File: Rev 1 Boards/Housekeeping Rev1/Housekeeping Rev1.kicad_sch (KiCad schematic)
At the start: 0 parts

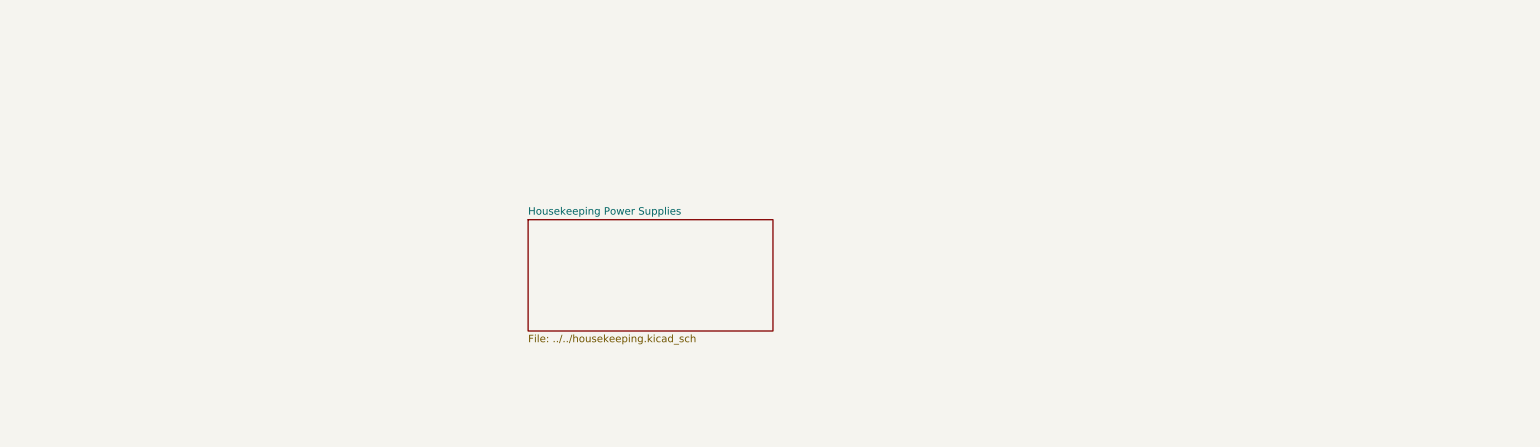
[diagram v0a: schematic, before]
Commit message: added footprints to prepare for pcb layout
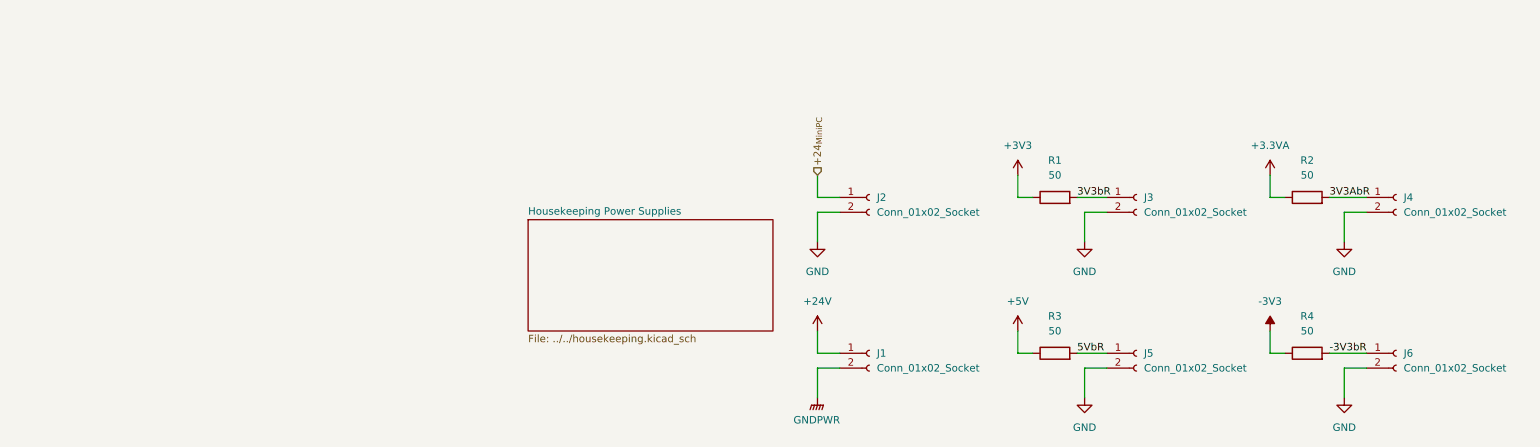
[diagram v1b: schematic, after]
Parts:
- added J1, J2: Conn_01x02_Socket, Connector:Banana_Jack_2Pin, symbol Connector:Conn_01x02_Socket
- added J3, J4, J5, J6: Conn_01x02_Socket, symbol Connector:Conn_01x02_Socket
- added R1, R2, R3, R4: 50, symbol Device:R
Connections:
- new net +24V: J1.1 (Pin_1)
- new net +24_{MiniPC}: J2.1 (Pin_1)
- new net +3.3VA: R2.1
- new net +3V3: R1.1
- new net +5V: R3.1
- new net -3V3: R4.1
- new net -3V3bR: J6.1 (Pin_1), R4.2
- new net 3V3AbR: J4.1 (Pin_1), R2.2
- new net 3V3bR: J3.1 (Pin_1), R1.2
- new net 5VbR: J5.1 (Pin_1), R3.2
- new net GND: J2.2 (Pin_2), J3.2 (Pin_2), J4.2 (Pin_2), J5.2 (Pin_2), J6.2 (Pin_2)
- new net GNDPWR: J1.2 (Pin_2)

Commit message: assigned footprints, mouser part numbers, and datasheets for passive components
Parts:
- J3, J4, J5, J6: footprint (none) -> Connector:Banana_Jack_2Pin
- R1, R2, R3, R4: footprint (none) -> Resistor_SMD:R_0201_0603Metric_Pad0.64x0.40mm_HandSolder; Mouser Part Number (none) -> 71-TNPW060350R0DEEA
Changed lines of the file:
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@@
 			)
 		)
-		(property "Footprint" ""
+		(property "Footprint" "Resistor_SMD:R_0201_0603Metric_Pad0.64x0.40mm_HandSolder"
 			(at 187.96 102.108 90)
 			(effects
@@
 			)
 		)
-		(property "Datasheet" "~"
+		(property "Datasheet" "https://www.vishay.com/docs/28758/tnpw_e3.pdf"
 			(at 187.96 100.33 0)
 			(effects
@@
 			)
 		)
+		(property "Mouser Part Number" "71-TNPW060350R0DEEA"
+			(at 187.96 100.33 0)
+			(effects
+				(font
+					(size 1.27 1.27)
+				)
+				(hide yes)
+			)
+		)
 		(pin "1"
 		)
@@
 			)
 		)
-		(property "Footprint" ""
+		(property "Footprint" "Resistor_SMD:R_0201_0603Metric_Pad0.64x0.40mm_HandSolder"
 			(at 187.96 75.438 90)
 			(effects
@@
 			)
 		)
-		(property "Datasheet" "~"
+		(property "Datasheet" "https://www.vishay.com/docs/28758/tnpw_e3.pdf"
 			(at 187.96 73.66 0)
 			(effects
@@
 			)
 		)
+		(property "Mouser Part Number" "71-TNPW060350R0DEEA"
+			(at 187.96 73.66 0)
+			(effects
+				(font
+					(size 1.27 1.27)
+				)
+				(hide yes)
+			)
+		)
 		(pin "1"
 		)
@@
 			)
 		)
-		(property "Footprint" ""
+		(property "Footprint" "Connector:Banana_Jack_2Pin"
 			(at 246.38 100.33 0)
 			(effects
@@
 			)
 		)
-		(property "Footprint" ""
+		(property "Footprint" "Resistor_SMD:R_0201_0603Metric_Pad0.64x0.40mm_HandSolder"
 			(at 231.14 102.108 90)
 			(effects
@@
 			)
 		)
-		(property "Datasheet" "~"
+		(property "Datasheet" "https://www.vishay.com/docs/28758/tnpw_e3.pdf"
 			(at 231.14 100.33 0)
 			(effects
@@
 			)
 		)
+		(property "Mouser Part Number" "71-TNPW060350R0DEEA"
+			(at 231.14 100.33 0)
+			(effects
+				(font
+					(size 1.27 1.27)
+				)
+				(hide yes)
+			)
+		)
 		(pin "1"
 		)
@@
 			)
 		)
-		(property "Footprint" ""
+		(property "Footprint" "Connector:Banana_Jack_2Pin"
 			(at 201.93 100.33 0)
 			(effects
@@
 			)
 		)
-		(property "Footprint" ""
+		(property "Footprint" "Connector:Banana_Jack_2Pin"
 			(at 246.38 73.66 0)
 			(effects
@@
 			)
 		)
-		(property "Footprint" ""
+		(property "Footprint" "Connector:Banana_Jack_2Pin"
 			(at 201.93 73.66 0)
 			(effects
@@
 			)
 		)
-		(property "Footprint" ""
+		(property "Footprint" "Resistor_SMD:R_0201_0603Metric_Pad0.64x0.40mm_HandSolder"
 			(at 231.14 75.438 90)
 			(effects
@@
 			)
 		)
-		(property "Datasheet" "~"
+		(property "Datasheet" "https://www.vishay.com/docs/28758/tnpw_e3.pdf"
 			(at 231.14 73.66 0)
 			(effects
@@
 			(at 231.14 73.66 0)
 			(effects
+				(font
+					(size 1.27 1.27)
+				)
+				(hide yes)
+			)
+		)
+		(property "Mouser Part Number" "71-TNPW060350R0DEEA"
+			(at 231.14 73.66 0)
+			(effects

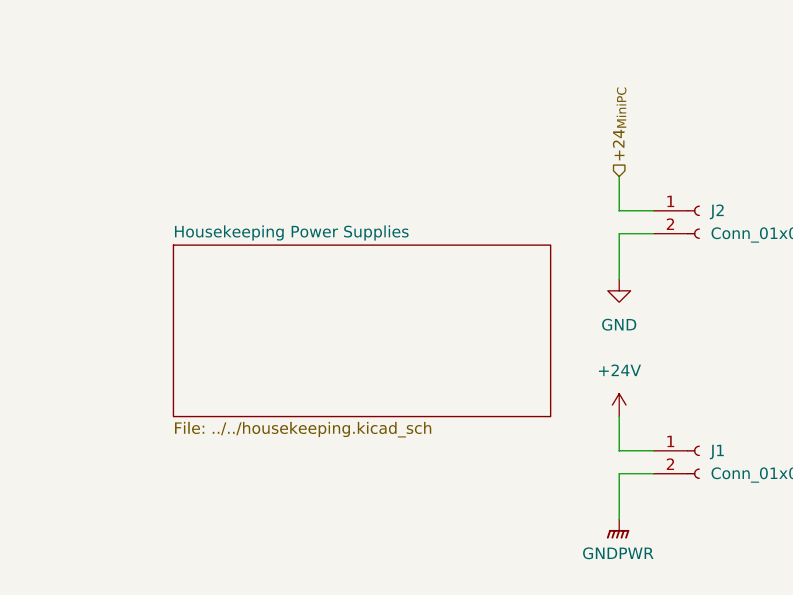
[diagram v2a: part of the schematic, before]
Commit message: beginning layout work for housekeeping pcb
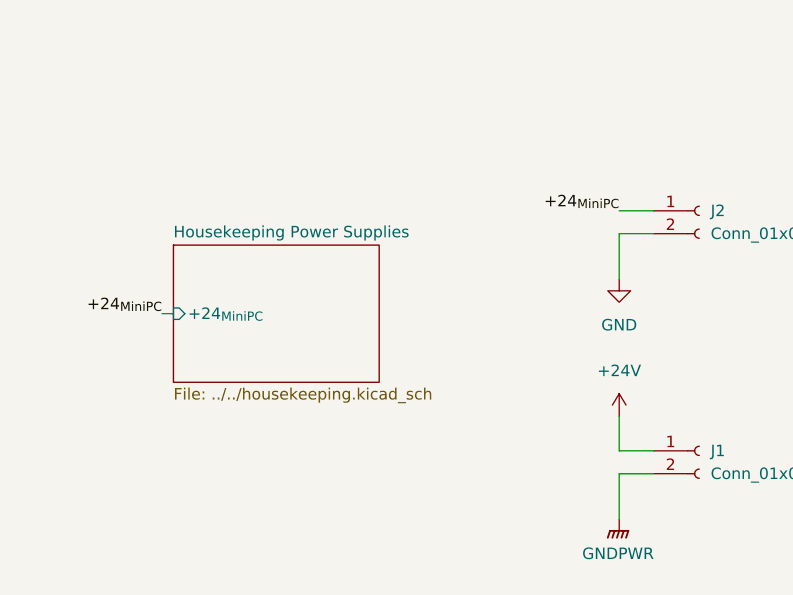
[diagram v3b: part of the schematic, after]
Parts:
- R1, R2, R3, R4: footprint Resistor_SMD:R_0201_0603Metric_Pad0.64x0.40mm_HandSolder -> Resistor_SMD:R_0603_1608Metric_Pad0.98x0.95mm_HandSolder
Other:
- sheet Housekeeping Power Supplies ports: added +24_{MiniPC}; removed none
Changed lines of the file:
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@@
-	(wire
-		(pts
-			(xy 147.32 69.85) (xy 147.32 73.66)
-		)
-		(stroke
-			(width 0)
-			(type default)
-		)
-	)
 	(wire
 		(pts
@@
 		(pts
 			(xy 237.49 102.87) (xy 237.49 107.95)
+		)
+		(stroke
+			(width 0)
+			(type default)
+		)
+	)
+	(wire
+		(pts
+			(xy 96.52 85.09) (xy 97.79 85.09)
 		)
 		(stroke
@@
 		)
 	)
+	(label "+24_{MiniPC}"
+		(at 96.52 85.09 180)
+		(effects
+			(font
+				(size 1.27 1.27)
+			)
+			(justify right bottom)
+		)
+	)
 	(label "5VbR"
 		(at 191.77 100.33 0)
@@
 		)
 	)
-	(hierarchical_label "+24_{MiniPC}"
-		(shape input)
-		(at 147.32 69.85 90)
+	(label "+24_{MiniPC}"
+		(at 147.32 73.66 180)
 		(effects
 			(font
 				(size 1.27 1.27)
 			)
-			(justify left)
+			(justify right bottom)
 		)
 	)
@@
 			)
 		)
-		(property "Footprint" "Resistor_SMD:R_0201_0603Metric_Pad0.64x0.40mm_HandSolder"
+		(property "Footprint" "Resistor_SMD:R_0603_1608Metric_Pad0.98x0.95mm_HandSolder"
 			(at 187.96 102.108 90)
 			(effects
@@
 			)
 		)
-		(property "Footprint" "Resistor_SMD:R_0201_0603Metric_Pad0.64x0.40mm_HandSolder"
+		(property "Footprint" "Resistor_SMD:R_0603_1608Metric_Pad0.98x0.95mm_HandSolder"
 			(at 187.96 75.438 90)
 			(effects
@@
 			)
 		)
-		(property "Footprint" "Resistor_SMD:R_0201_0603Metric_Pad0.64x0.40mm_HandSolder"
+		(property "Footprint" "Resistor_SMD:R_0603_1608Metric_Pad0.98x0.95mm_HandSolder"
 			(at 231.14 102.108 90)
 			(effects
@@
 			)
 		)
-		(property "Footprint" "Resistor_SMD:R_0201_0603Metric_Pad0.64x0.40mm_HandSolder"
+		(property "Footprint" "Resistor_SMD:R_0603_1608Metric_Pad0.98x0.95mm_HandSolder"
 			(at 231.14 75.438 90)
 			(effects
@@
 	(sheet
 		(at 97.79 77.47)
-		(size 41.91 19.05)
+		(size 22.86 15.24)
 		(exclude_from_sim no)
 		(in_bom yes)
@@
 		)
 		(property "Sheetfile" "../../housekeeping.kicad_sch"
-			(at 97.79 97.1046 0)
+			(at 97.79 93.2946 0)
 			(effects
 				(font
@@
 			)
 		)
+		(pin "+24_{MiniPC}" input
+			(at 97.79 85.09 180)
+			(effects
+				(font
+					(size 1.27 1.27)
+				)
+				(justify left)
+			)
+		)

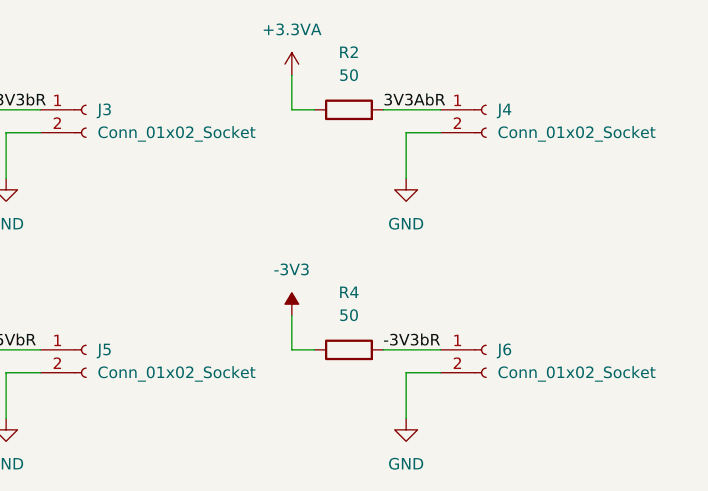
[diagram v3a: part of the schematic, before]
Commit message: began pcb layout ofr housekeeping
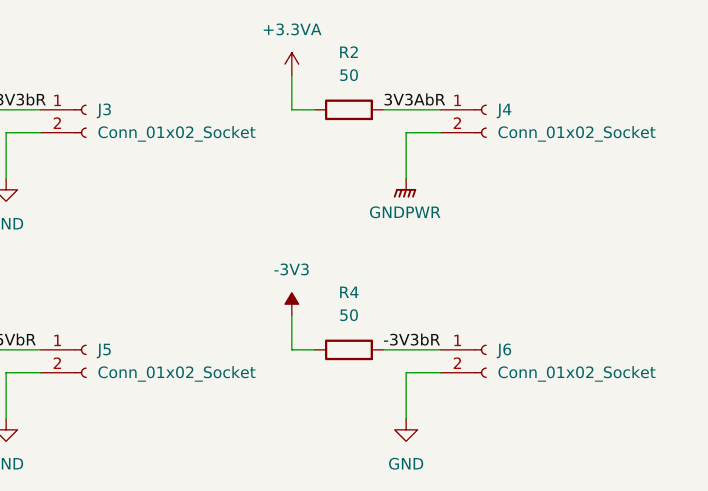
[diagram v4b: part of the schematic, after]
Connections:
- net GND: no longer J4.2 (Pin_2)
- net GNDPWR: now also J4.2 (Pin_2)
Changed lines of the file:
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@@
+	)
+	(symbol
+		(lib_id "power:GNDPWR")
+		(at 237.49 81.28 0)
+		(unit 1)
+		(exclude_from_sim no)
+		(in_bom yes)
+		(on_board yes)
+		(dnp no)
+		(fields_autoplaced yes)
+		(property "Reference" "#PWR07"
+			(at 237.49 86.36 0)
+			(effects
+				(font
+					(size 1.27 1.27)
+				)
+				(hide yes)
+			)
+		)
+		(property "Value" "GNDPWR"
+			(at 237.363 85.09 0)
+			(effects
+				(font
+					(size 1.27 1.27)
+				)
+			)
+		)
+		(property "Footprint" ""
+			(at 237.49 82.55 0)
+			(effects
+				(font
+					(size 1.27 1.27)
+				)
+				(hide yes)
+			)
+		)
+		(property "Datasheet" ""
+			(at 237.49 82.55 0)
+			(effects
+				(font
+					(size 1.27 1.27)
+				)
+				(hide yes)
+			)
+		)
+		(property "Description" "Power symbol creates a global label with name \"GNDPWR\" , global ground"
+			(at 237.49 81.28 0)
+			(effects
+				(font
+					(size 1.27 1.27)
+				)
+				(hide yes)
+			)
+		)
+		(pin "1"
+		)
+		(instances
+			(project "Housekeeping Rev1"
+				(path "/d2a5f610-b666-4f42-b17a-f8b6e55a52c2"
+					(reference "#PWR07")
+					(unit 1)
+				)
+			)
+		)
 	)
 	(symbol
@@
 					(unit 1)
 				)
-			)
-		)
-	)
-	(symbol
-		(lib_id "power:GND")
-		(at 237.49 81.28 0)
-		(unit 1)
-		(exclude_from_sim no)
-		(in_bom yes)
-		(on_board yes)
-		(dnp no)
-		(fields_autoplaced yes)
-		(property "Reference" "#PWR07"
-			(at 237.49 87.63 0)
-			(effects
-				(font
-					(size 1.27 1.27)
-				)
-				(hide yes)
-			)
-		)
-		(property "Value" "GND"
-			(at 237.49 86.36 0)
-			(effects
-				(font
-					(size 1.27 1.27)
-				)
-			)
-		)
-		(property "Footprint" ""
-			(at 237.49 81.28 0)
-			(effects
-				(font
-					(size 1.27 1.27)
-				)
-				(hide yes)
-			)
-		)
-		(property "Datasheet" ""
-			(at 237.49 81.28 0)
-			(effects
-				(font
-					(size 1.27 1.27)
-				)
-				(hide yes)
-			)
-		)
-		(property "Description" "Power symbol creates a global label with name \"GND\" , ground"
-			(at 237.49 81.28 0)
-			(effects
-				(font
-					(size 1.27 1.27)
-				)
-				(hide yes)
-			)
-		)
-		(pin "1"
-		)
-		(instances
-			(project "Housekeeping Rev1"
-				(path "/d2a5f610-b666-4f42-b17a-f8b6e55a52c2"
-					(reference "#PWR07")
-					(unit 1)
-				)

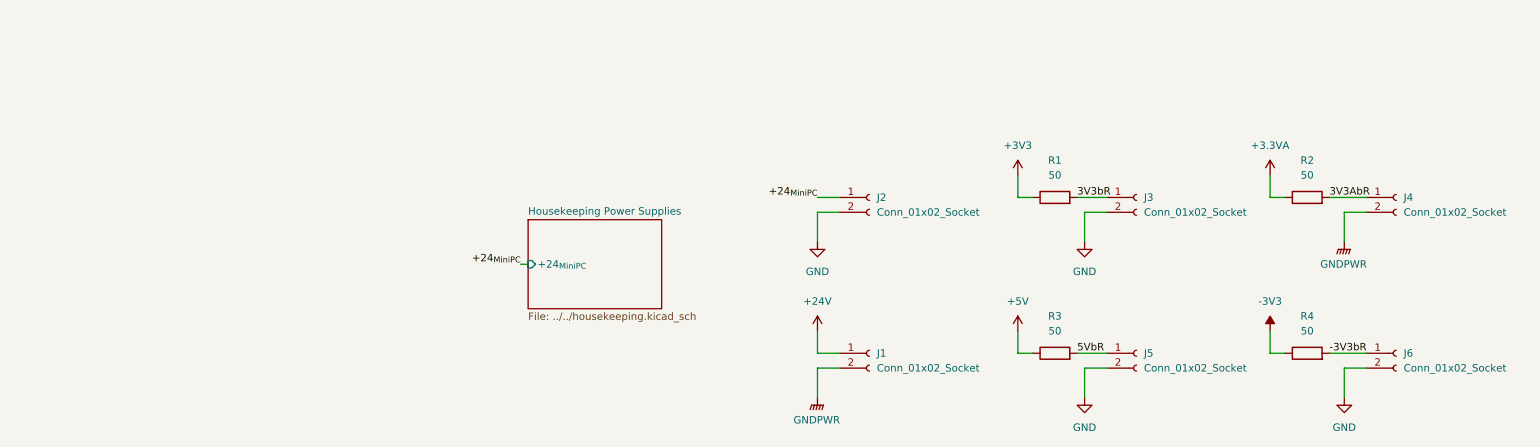
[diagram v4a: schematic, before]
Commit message: Created preliminary board layout for dev board interface pcb, pending review by Jed
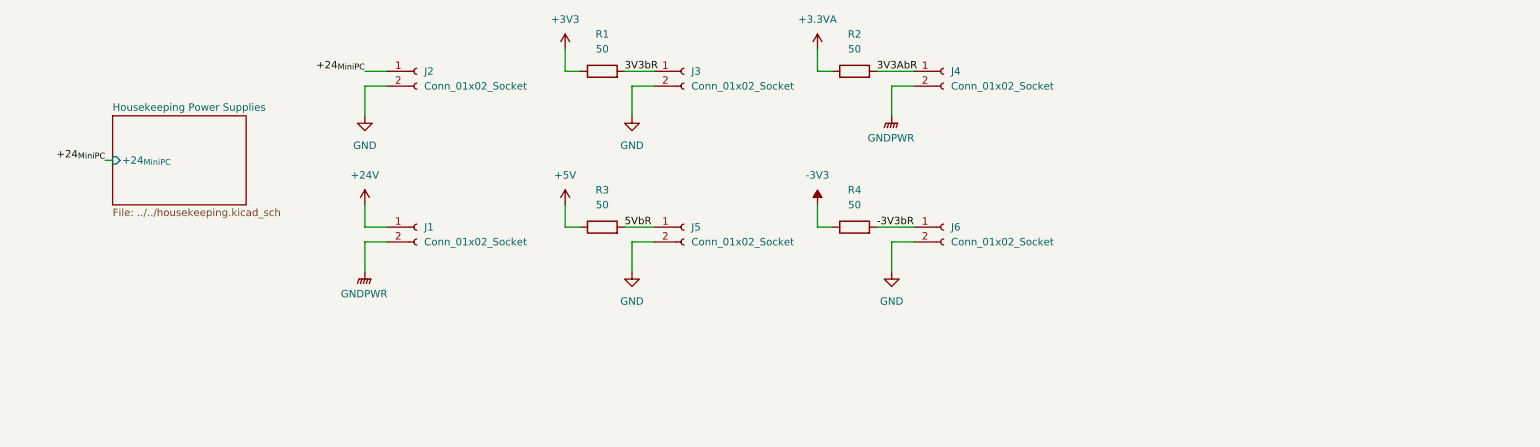
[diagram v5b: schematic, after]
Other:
- moved on the sheet: J1, J2, J3, J4, J5, J6, R1, R2, R3, R4
